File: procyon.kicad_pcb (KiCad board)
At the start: 4 copper layers, 49.6 x 42 mm, 26 parts, among them J1 Conn_01x07_Pin, Q1 AO3401A, U1 mXT336UD-MAU002

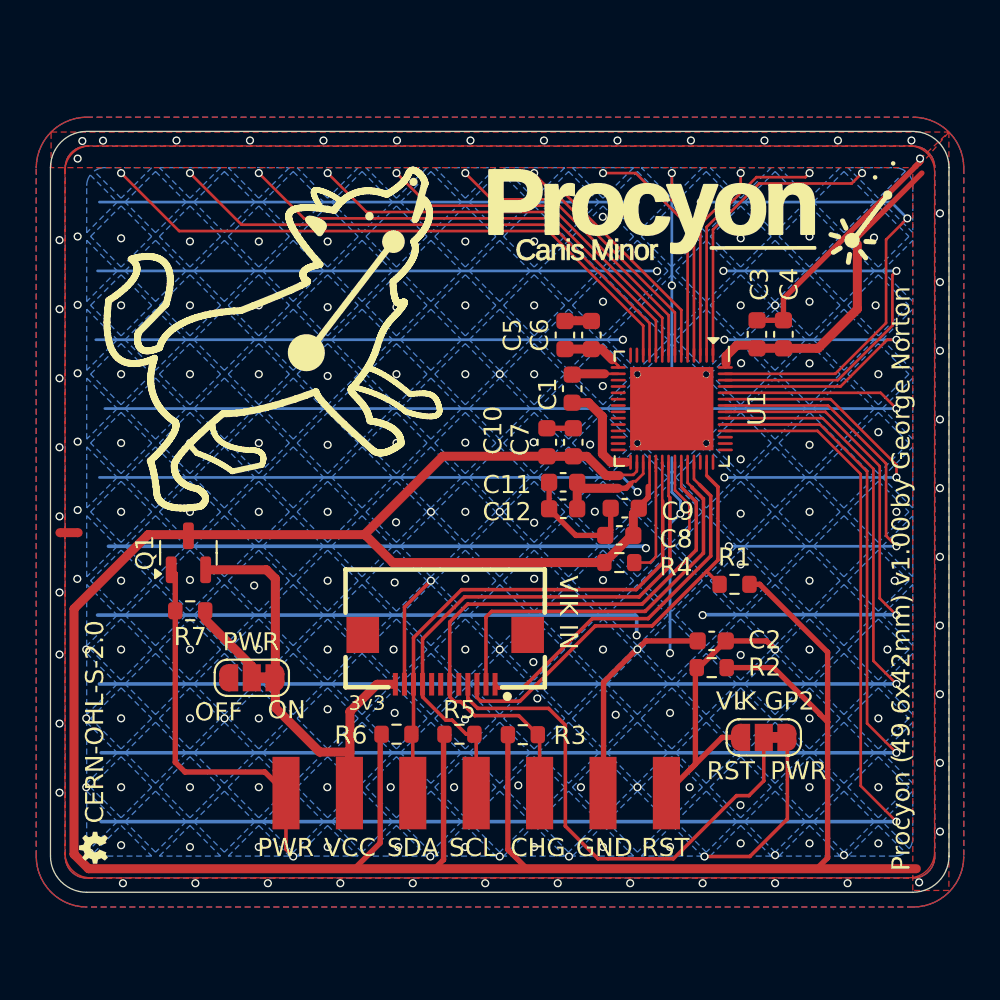
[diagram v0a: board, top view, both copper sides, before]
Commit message: Swap from a 12x10 to a 10x12 matrix so we can use self capacitance measurements.
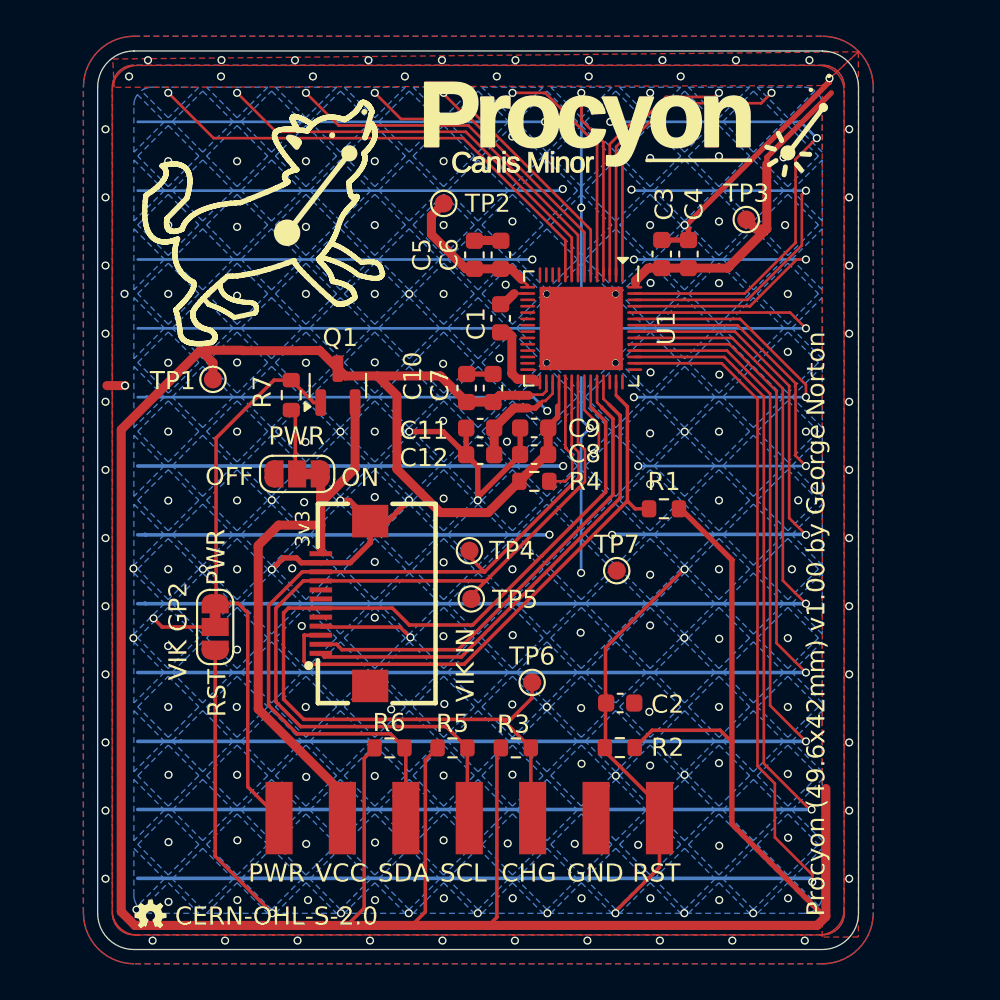
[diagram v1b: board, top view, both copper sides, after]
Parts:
- added TP1: TestPoint, TestPoint:TestPoint_Pad_D1.0mm, F.Cu at (84.2, 67.3)
- added TP2: TestPoint, TestPoint:TestPoint_Pad_D1.0mm, F.Cu at (96.9, 57.6)
- added TP3: TestPoint, TestPoint:TestPoint_Pad_D1.0mm, F.Cu at (113.6, 58.5)
- added TP4: TestPoint, TestPoint:TestPoint_Pad_D1.0mm, F.Cu at (98.3, 76.8)
- added TP5: TestPoint, TestPoint:TestPoint_Pad_D1.0mm, F.Cu at (98.4, 79.4)
- added TP6: TestPoint, TestPoint:TestPoint_Pad_D1.0mm, F.Cu at (101.8, 84.1)
- added TP7: TestPoint, TestPoint:TestPoint_Pad_D1.0mm, F.Cu at (106.4, 77.9)
- JP1: renamed from VIK GP2
- moved JP1 30.9 mm to (84.3, 81.0), turned to -90 degrees
- moved R7 13.1 mm to (88.5, 68.2), turned to 90 degrees
- moved Q1 12.4 mm to (91.1, 67.7)
- moved JP2 11.5 mm to (88.8, 72.5)
- moved NT1 8.52 mm to (78.8, 67.7)
- moved C3 6.88 mm to (108.9, 60.4)
- moved C4 6.86 mm to (110.4, 60.4)
- moved R2 6.72 mm to (106.6, 87.7)
- moved C5 6.68 mm to (98.6, 60.4)
- moved C6 6.68 mm to (100.0, 60.4)
- moved C9 6.68 mm to (101.9, 70.0)
- moved U1 6.68 mm to (104.5, 64.5)
- moved R4 6.49 mm to (101.9, 73.0)
- moved C8 6.48 mm to (101.9, 71.5)
- moved C2 6.10 mm to (106.6, 85.2), turned to 0 degrees
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- renumbered PWR to JP2
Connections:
- net /Col1 renamed /Y0
- net /Col10 renamed /Y9
- net /Col2 renamed /Y1
- net /Col3 renamed /Y2
- net /Col4 renamed /Y3
- net /Col5 renamed /Y4
- net /Col6 renamed /Y5
- net /Col7 renamed /Y6
- net /Col8 renamed /Y7
- net /Col9 renamed /Y8
- net /Row1 renamed /X0
- net /Row10 renamed /X9
- net /Row2 renamed /X1
- net /Row3 renamed /X2
- net /Row4 renamed /X3
- net /Row5 renamed /X4
- net /Row6 renamed /X5
- net /Row7 renamed /X6
- net /Row8 renamed /X7
- net /Row9 renamed /X8
- net Net-(U1-XVDD) renamed /XVDD
- U1 pad 11: /Row11 -> unconnected-(U1-X10-Pad11)
- U1 pad 12: /Row12 -> unconnected-(U1-X11-Pad12)
- U1 pad 40: /DBG_SS -> unconnected-(U1-DS0-Pad40)
- U1 pad 41: unconnected-(U1-GPIO3-Pad41) -> /DBG_SS
- U1 pad 43: (no net) -> unconnected-(U1-GPIO4-Pad43)
- U1 pad 44: unconnected-(U1-Y11-Pad44) -> /Y11
- U1 pad 45: unconnected-(U1-Y10-Pad45) -> /Y10
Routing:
- net /Y11: track 0.00 -> 72.7 mm, vias 0 -> 1
- net /Row12: track 71.0 -> 0.00 mm, vias 11 -> 0
- net /Y10: track 0.00 -> 69.2 mm, vias 0 -> 1
- net /Row11: track 67.8 -> 0.00 mm, vias 11 -> 0
- net /RESET: track 29.2 -> 71.3 mm, vias 2 -> 4
- net /POWER_CONTROL: track 54.5 -> 30.8 mm, vias 2 -> 0
- net /CHANGE: track 33.6 -> 54.2 mm
- net +3.3V: track 184.9 -> 204.8 mm
- net /SCL: track 31.3 -> 47.7 mm
- net /SDA: track 29.7 -> 44.9 mm
- net /Y6: track 64.6 -> 55.3 mm
- net /DBG_SS: track 24.0 -> 32.2 mm
- net /X2: track 48.0 -> 56.0 mm, vias 11 -> 13
- net /X7: track 59.0 -> 66.8 mm, vias 11 -> 13
- net /X1: track 51.0 -> 58.6 mm, vias 11 -> 13
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- added copper zone on B.Cu, net /Y10
- added copper zone on B.Cu, net /Y11
- removed copper zone on B.Cu, net /Row11
- removed copper zone on B.Cu, net /Row12
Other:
- board size 49.6 x 42 mm -> 42 x 49.6 mm
- board text added: "I am not an EE, but I have read some application notes. I have done some things with the routing which make sense to me, if you change the routing bare in mind: - Running sensor lines close to ground will generate some paracitic capacitance and reduce the sensitivity of those lines. - Running TX lines close to RX lines will also generate paracitic capacitance, but it will be detected by the recei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"
- board text added: "VIK GP2"

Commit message: Add TP8.
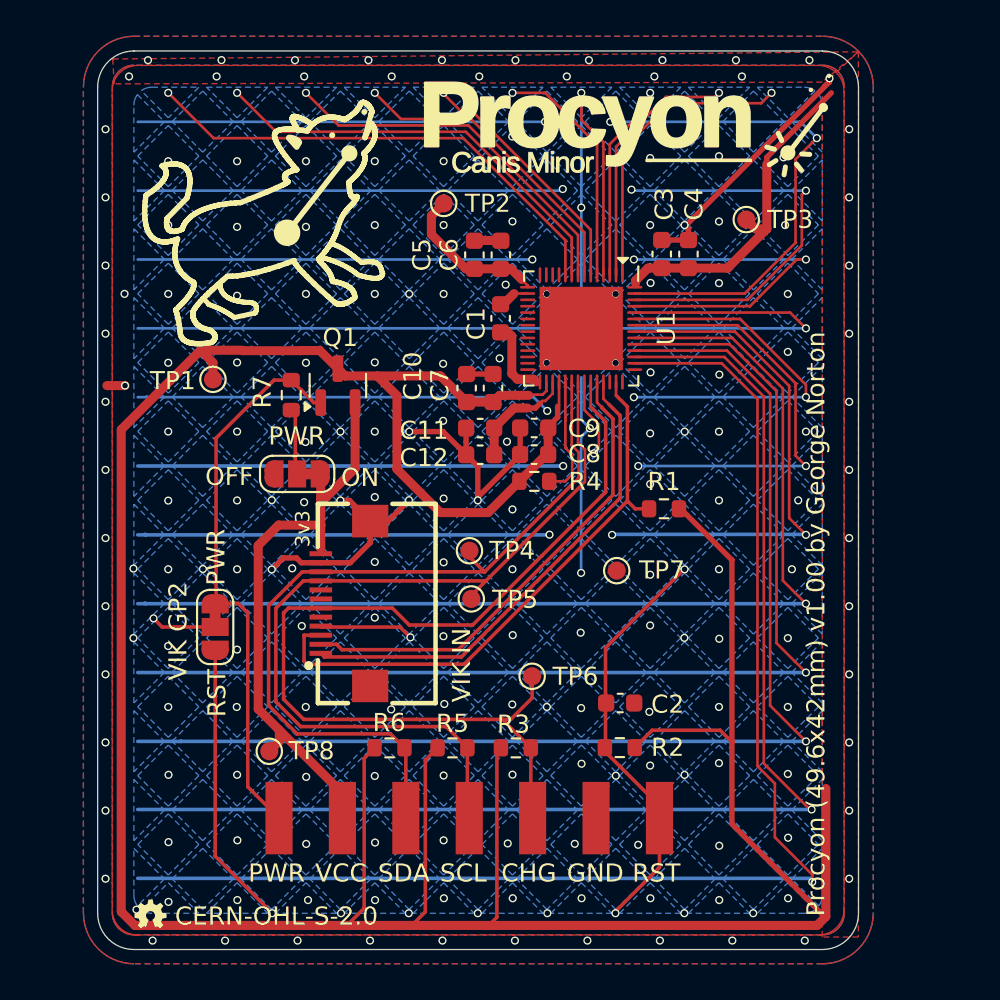
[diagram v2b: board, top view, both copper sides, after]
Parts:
- added TP8: TestPoint, TestPoint:TestPoint_Pad_D1.0mm, F.Cu at (87.3, 87.9)
- moved TP6 0.34 mm to (101.8, 83.7)
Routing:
- net +3V3 IN: track 31.3 -> 32.7 mm
- net GND: vias 34 -> 35
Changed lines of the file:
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@@
 		)
 	)
+	(footprint "TestPoint:TestPoint_Pad_D1.0mm"
+		(layer "F.Cu")
+		(at 87.265 87.855)
+		(descr "SMD pad as test Point, diameter 1.0mm")
+		(tags "test point SMD pad")
+		(property "Reference" "TP8"
+			(at 2.329325 -0.019103 0)
+			(layer "F.SilkS")
+			(effects
+				(font
+					(size 1 1)
+					(thickness 0.15)
+				)
+			)
+		)
+		(property "Value" "TestPoint"
+			(at 0 1.55 0)
+			(layer "F.Fab")
+			(effects
+				(font
+					(size 1 1)
+					(thickness 0.15)
+				)
+			)
+		)
+		(property "Footprint" "TestPoint:TestPoint_Pad_D1.0mm"
+			(at 0 0 0)
+			(unlocked yes)
+			(layer "F.Fab")
+			(hide yes)
+			(effects
+				(font
+					(size 1.27 1.27)
+					(thickness 0.15)
+				)
+			)
+		)
+		(property "Datasheet" ""
+			(at 0 0 0)
+			(unlocked yes)
+			(layer "F.Fab")
+			(hide yes)
+			(effects
+				(font
+					(size 1.27 1.27)
+					(thickness 0.15)
+				)
+			)
+		)
+		(property "Description" "test point"
+			(at 0 0 0)
+			(unlocked yes)
+			(layer "F.Fab")
+			(hide yes)
+			(effects
+				(font
+					(size 1.27 1.27)
+					(thickness 0.15)
+				)
+			)
+		)
+		(property ki_fp_filters "Pin* Test*")
+		(sheetname "Root")
+		(sheetfile "procyon.kicad_sch")
+		(attr exclude_from_pos_files)
+		(fp_circle
+			(center 0 0)
+			(end 0 0.7)
+			(stroke
+				(width 0.12)
+				(type solid)
+			)
+			(fill none)
+			(layer "F.SilkS")
+		)
+		(fp_circle
+			(center 0 0)
+			(end 1 0)
+			(stroke
+				(width 0.05)
+				(type solid)
+			)
+			(fill none)
+			(layer "F.CrtYd")
+		)
+		(fp_text user "${REFERENCE}"
+			(at 0 -1.45 0)
+			(layer "F.Fab")
+			(effects
+				(font
+					(size 1 1)
+					(thickness 0.15)
+				)
+			)
+		)
+		(pad "1" smd circle
+			(at 0 0)
+			(size 1 1)
+			(layers "F.Cu" "F.Mask")
+			(net 3 "+3V3 IN")
+			(pinfunction "1")
+			(pintype "passive")
+		)
+	)
 	(footprint "Capacitor_SMD:C_0603_1608Metric"
 		(layer "F.Cu")
@@
 	(footprint "TestPoint:TestPoint_Pad_D1.0mm"
 		(layer "F.Cu")
-		(at 101.774325 84.055897)
+		(at 101.774325 83.715897)
 		(descr "SMD pad as test Point, diameter 1.0mm")
 		(tags "test point SMD pad")
 		(property "Reference" "TP6"
-			(at 0 -1.448 0)
+			(at 2.39 0.01 0)
 			(layer "F.SilkS")
 			(effects
@@
 		(tags "test point SMD pad")
 		(property "Reference" "TP3"
-			(at 0 -1.448 0)
+			(at 2.42 0 0)
 			(layer "F.SilkS")
 			(effects
@@
 		(tags "test point SMD pad")
 		(property "Reference" "TP7"
-			(at 0 -1.448 0)
+			(at 2.5 -0.03 0)
 			(layer "F.SilkS")
 			(effects
@@
 		)
 		(fp_text user "VIK IN"
-			(at -5.455896 6.526405 90)
+			(at -5.455896 6.316405 90)
 			(unlocked yes)
 			(layer "F.SilkS" knockout)
@@
 	)
 	(via
-		(at 99.824325 50.605897)
+		(at 98.856109 50.605897)
 		(size 0.45)
 		(drill 0.3)
@@
 	)
 	(via
-		(at 94.749325 50.605897)
+		(at 94.023163 50.605897)
 		(size 0.45)
 		(drill 0.3)
@@
 	)
 	(via
-		(at 89.674325 50.605897)
+		(at 89.190217 50.605897)
 		(size 0.45)
 		(drill 0.3)
@@
 	)
 	(via
+		(at 113.354947 50.605897)
+		(size 0.45)
+		(drill 0.3)
+		(layers "F.Cu" "B.Cu")
+		(remove_unused_layers yes)
+		(keep_end_layers yes)
+		(free yes)
+		(zone_layer_connections "In1.Cu")
+		(net 1)
+	)
+	(via
 		(at 110.194325 70.215897)
 		(size 0.45)
@@
 	)
 	(via
-		(at 109.974325 50.605897)
+		(at 108.522001 50.605897)
 		(size 0.45)
 		(drill 0.3)
@@
 	)
 	(via
-		(at 104.899325 50.605897)
+		(at 103.689055 50.605897)
 		(size 0.45)
 		(drill 0.3)
@@
 	)
 	(via
-		(at 84.599325 50.605897)
+		(at 84.357271 50.605897)
 		(size 0.45)
 		(drill 0.3)
@@
 	)
 	(segment
+		(start 86.652099 85.522838)
+		(end 87.819741 86.690481)
+		(width 0.5)
+		(layer "F.Cu")
+		(net 3)
+	)
+	(segment
 		(start 90.10992 75.37002)
 		(end 87.777099 75.37002)
@@
 	)
 	(segment
+		(start 87.819741 87.300259)
+		(end 87.819741 86.690481)
+		(width 0.5)
+		(layer "F.Cu")
+		(net 3)
+	)
+	(segment
 		(start 90.102099 73.854378)
 		(end 90.102099 72.54502)
@@
 	)
 	(segment
+		(start 87.819741 86.690481)
+		(end 91.302099 90.172838)
+		(width 0.5)
+		(layer "F.Cu")
+		(net 3)
+	)
+	(segment
 		(start 90.10992 75.37002)
 		(end 90.10992 76.662199)
@@
 	)
 	(segment
-		(start 86.652099 85.522838)
-		(end 91.302099 90.172838)
+		(start 87.265 87.855)
+		(end 87.819741 87.300259)
 		(width 0.5)
 		(layer "F.Cu")
@@
 	)
 	(segment
-		(start 100.594562 86.09502)
-		(end 101.774325 84.915257)
+		(start 102.305721 77.069339)
+		(end 98.489163 80.885897)
 		(width 0.2)
 		(layer "F.Cu")
@@
 	)
 	(segment
-		(start 102.305721 77.069339)
-		(end 98.489163 80.885897)
+		(start 101.774325 84.915257)
+		(end 101.774325 83.715897)
 		(width 0.2)
 		(layer "F.Cu")
@@
 	)
 	(segment
-		(start 100.127119 86.09502)
-		(end 100.594562 86.09502)
+		(start 88.322118 79.950001)
+		(end 88.052099 80.22002)
 		(width 0.2)
 		(layer "F.Cu")
@@
 	)
 	(segment
-		(start 88.322118 79.950001)
-		(end 88.052099 80.22002)
+		(start 100.594562 86.09502)
+		(end 101.774325 84.915257)
 		(width 0.2)
 		(layer "F.Cu")
@@
 	)
 	(segment
-		(start 98.489163 80.885897)
-		(end 94.994325 80.885897)
+		(start 100.127119 86.09502)
+		(end 100.594562 86.09502)
 		(width 0.2)
 		(layer "F.Cu")
@@
 	)
 	(segment
-		(start 105.598585 73.776476)
-		(end 102.305721 77.069339)
+		(start 98.489163 80.885897)
+		(end 94.994325 80.885897)
 		(width 0.2)
 		(layer "F.Cu")
@@
 	)
 	(segment
-		(start 101.774325 84.915257)
-		(end 101.774325 84.055897)
+		(start 105.598585 73.776476)
+		(end 102.305721 77.069339)
 		(width 0.2)
 		(layer "F.Cu")
@@
 		(polygon
 			(pts
-				(xy 78.62221 49.644211) (xy 119.782002 49.244225) (xy 117.787899 51.1099) (xy 78.704325 51.205897)
+				(xy 78.62221 49.644211) (xy 119.782002 49.244225) (xy 117.787899 50.9199) (xy 78.704325 51.015897)
 			)
 		)
@@
 		(polygon
 			(pts
-				(xy 80.424325 51.405897) (xy 115.957899 51.2099) (xy 114.447899 52.6699) (xy 109.607899 52.6999)
+				(xy 80.414325 50.915897) (xy 116.654325 50.845897) (xy 114.447899 52.6699) (xy 109.607899 52.6999)
 				(xy 107.527899 54.9299) (xy 107.577899 62.2499) (xy 113.307899 62.2099) (xy 115.907899 59.5899)
 				(xy 115.887899 55.0899) (xy 117.727899 53.4599) (xy 117.627899 88.1499) (xy 116.407899 88.1799)
